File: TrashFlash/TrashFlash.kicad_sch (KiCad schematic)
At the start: 1 part, among them IC4 MCP4151-103E_MF

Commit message: Bevor new Shematic
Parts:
- removed IC4: MCP4151-103E_MF, SON65P300X300X100-9N-D, symbol TrashFlash:MCP4151-103E_MF
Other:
- added sheet MCU (MCU.kicad_sch)
- added sheet Supply (Supply.kicad_sch)
- sheet LED_Supply ports: added V_VOLTAGE_SET; removed POTY_CS, POTY_SCK, POTY_SDI/SDO

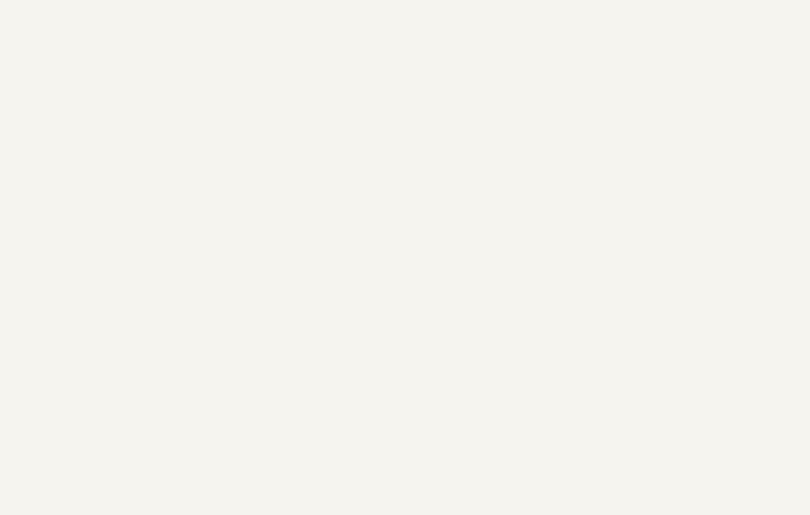
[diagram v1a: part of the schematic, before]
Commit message: Added RGB leds/driver for user interface
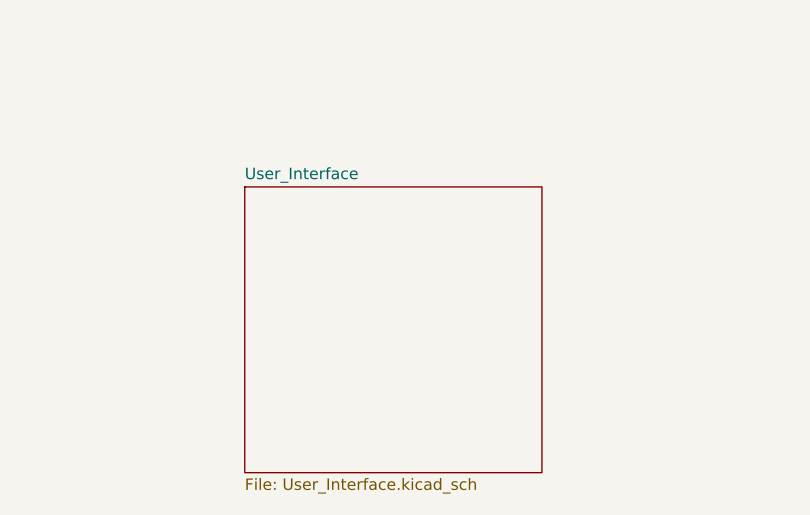
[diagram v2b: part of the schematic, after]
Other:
- added sheet User_Interface (User_Interface.kicad_sch)
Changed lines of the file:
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@@
+		)
+	)
+	(sheet
+		(at 121.92 124.46)
+		(size 33.02 31.75)
+		(exclude_from_sim no)
+		(in_bom yes)
+		(on_board yes)
+		(dnp no)
+		(fields_autoplaced yes)
+		(stroke
+			(width 0.1524)
+			(type solid)
+		)
+		(fill
+			(color 0 0 0 0.0000)
+		)
+		(property "Sheetname" "User_Interface"
+			(at 121.92 123.7484 0)
+			(effects
+				(font
+					(size 1.27 1.27)
+				)
+				(justify left bottom)
+			)
+		)
+		(property "Sheetfile" "User_Interface.kicad_sch"
+			(at 121.92 156.7946 0)
+			(effects
+				(font
+					(size 1.27 1.27)
+				)
+				(justify left top)
+			)
+		)
+		(instances
+			(project "TrashFlash"
+				(path "/256082dc-9c82-41ae-bfb7-0b4bd4121c78"
+					(page "6")
+				)
+			)
 		)
 	)

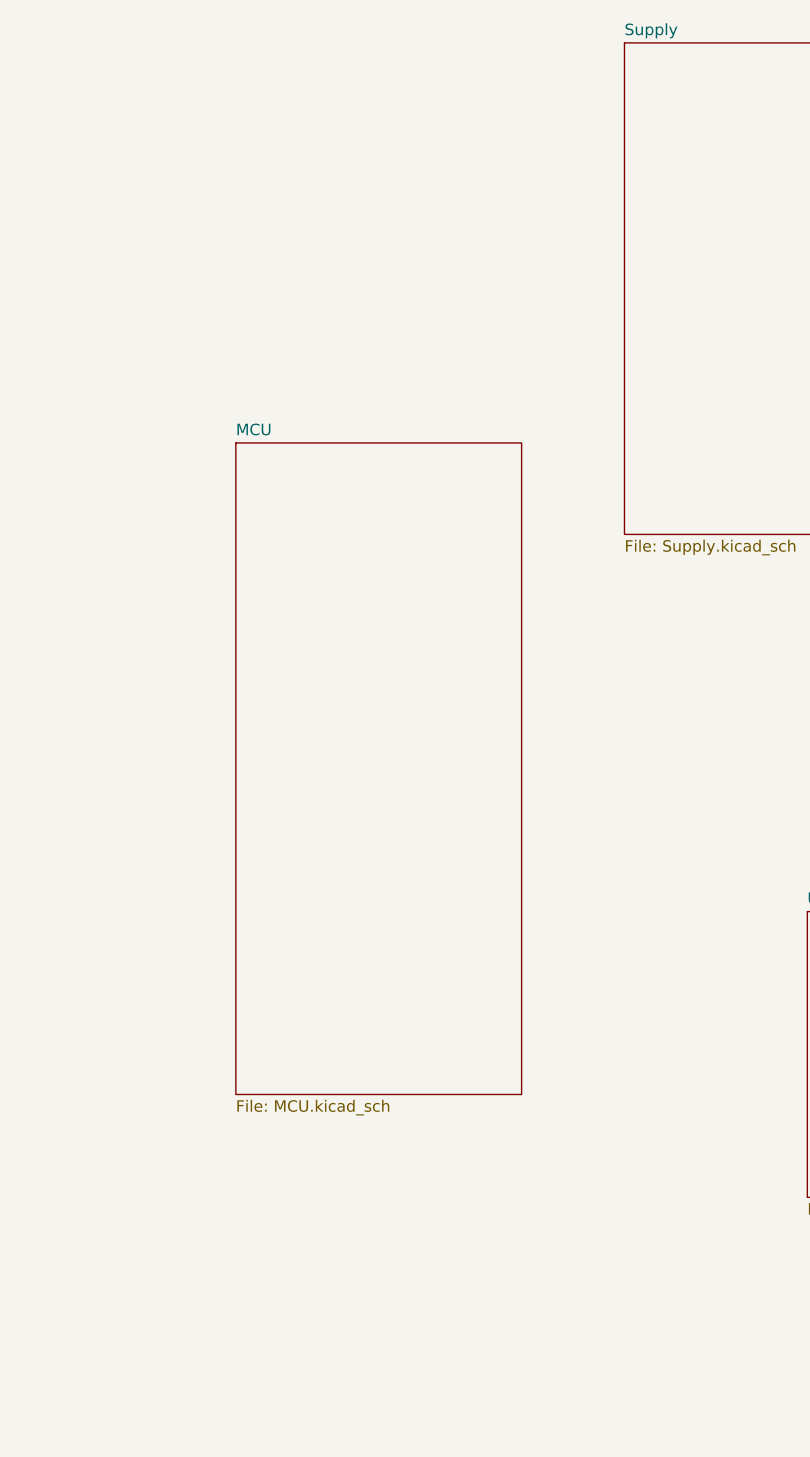
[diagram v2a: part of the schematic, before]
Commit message: Added Battery Management
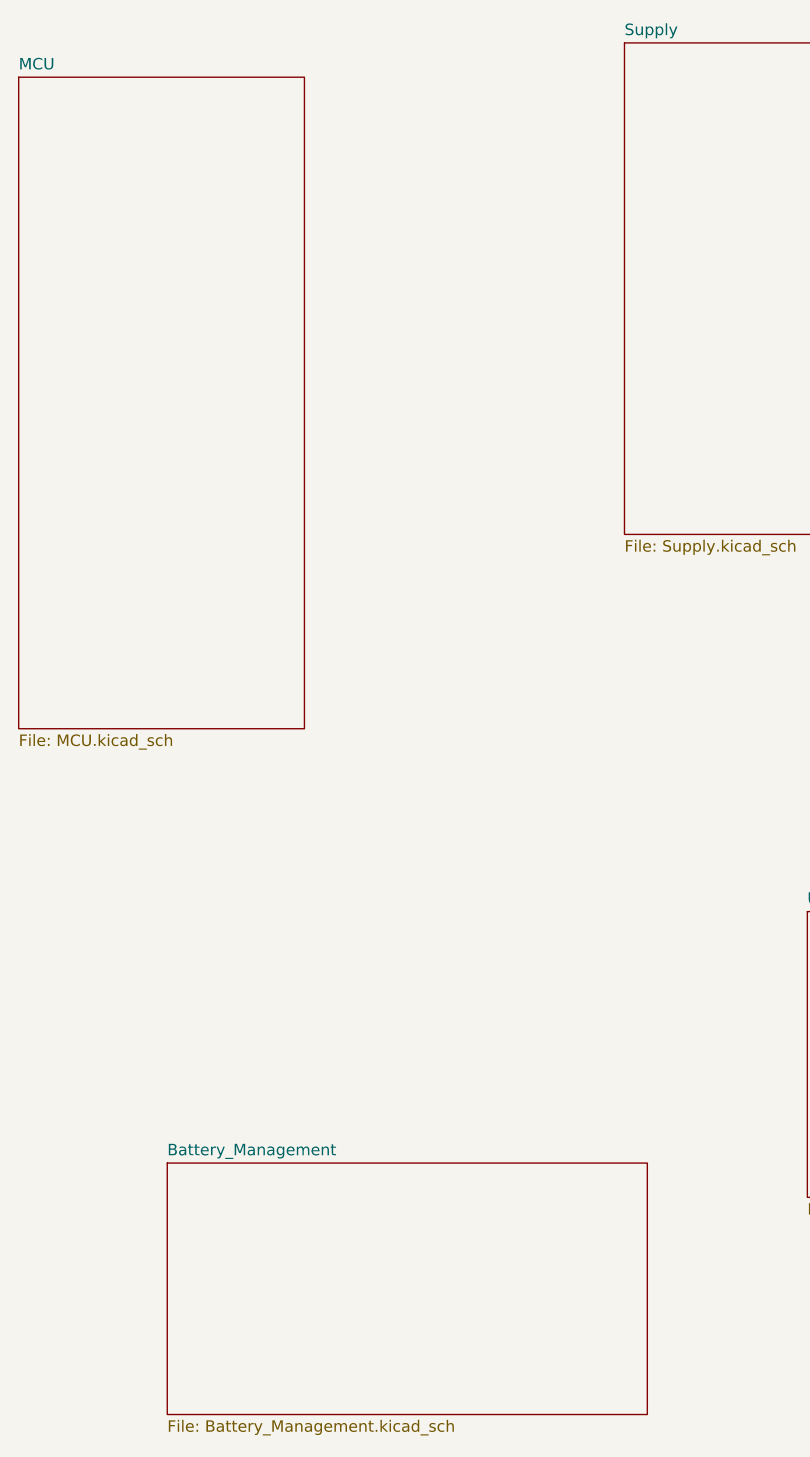
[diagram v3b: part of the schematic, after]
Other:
- added sheet Battery_Management (Battery_Management.kicad_sch)
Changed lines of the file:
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@@
 	)
 	(sheet
-		(at 58.42 72.39)
+		(at 50.8 152.4)
+		(size 53.34 27.94)
+		(exclude_from_sim no)
+		(in_bom yes)
+		(on_board yes)
+		(dnp no)
+		(fields_autoplaced yes)
+		(stroke
+			(width 0.1524)
+			(type solid)
+		)
+		(fill
+			(color 0 0 0 0.0000)
+		)
+		(property "Sheetname" "Battery_Management"
+			(at 50.8 151.6884 0)
+			(effects
+				(font
+					(size 1.27 1.27)
+				)
+				(justify left bottom)
+			)
+		)
+		(property "Sheetfile" "Battery_Management.kicad_sch"
+			(at 50.8 180.9246 0)
+			(effects
+				(font
+					(size 1.27 1.27)
+				)
+				(justify left top)
+			)
+		)
+		(instances
+			(project "TrashFlash"
+				(path "/256082dc-9c82-41ae-bfb7-0b4bd4121c78"
+					(page "7")
+				)
+			)
+		)
+	)
+	(sheet
+		(at 34.29 31.75)
 		(size 31.75 72.39)
 		(exclude_from_sim no)
@@
 		)
 		(property "Sheetname" "MCU"
-			(at 58.42 71.6784 0)
+			(at 34.29 31.0384 0)
 			(effects
 				(font
@@
 		)
 		(property "Sheetfile" "MCU.kicad_sch"
-			(at 58.42 145.3646 0)
+			(at 34.29 104.7246 0)
 			(effects
 				(font

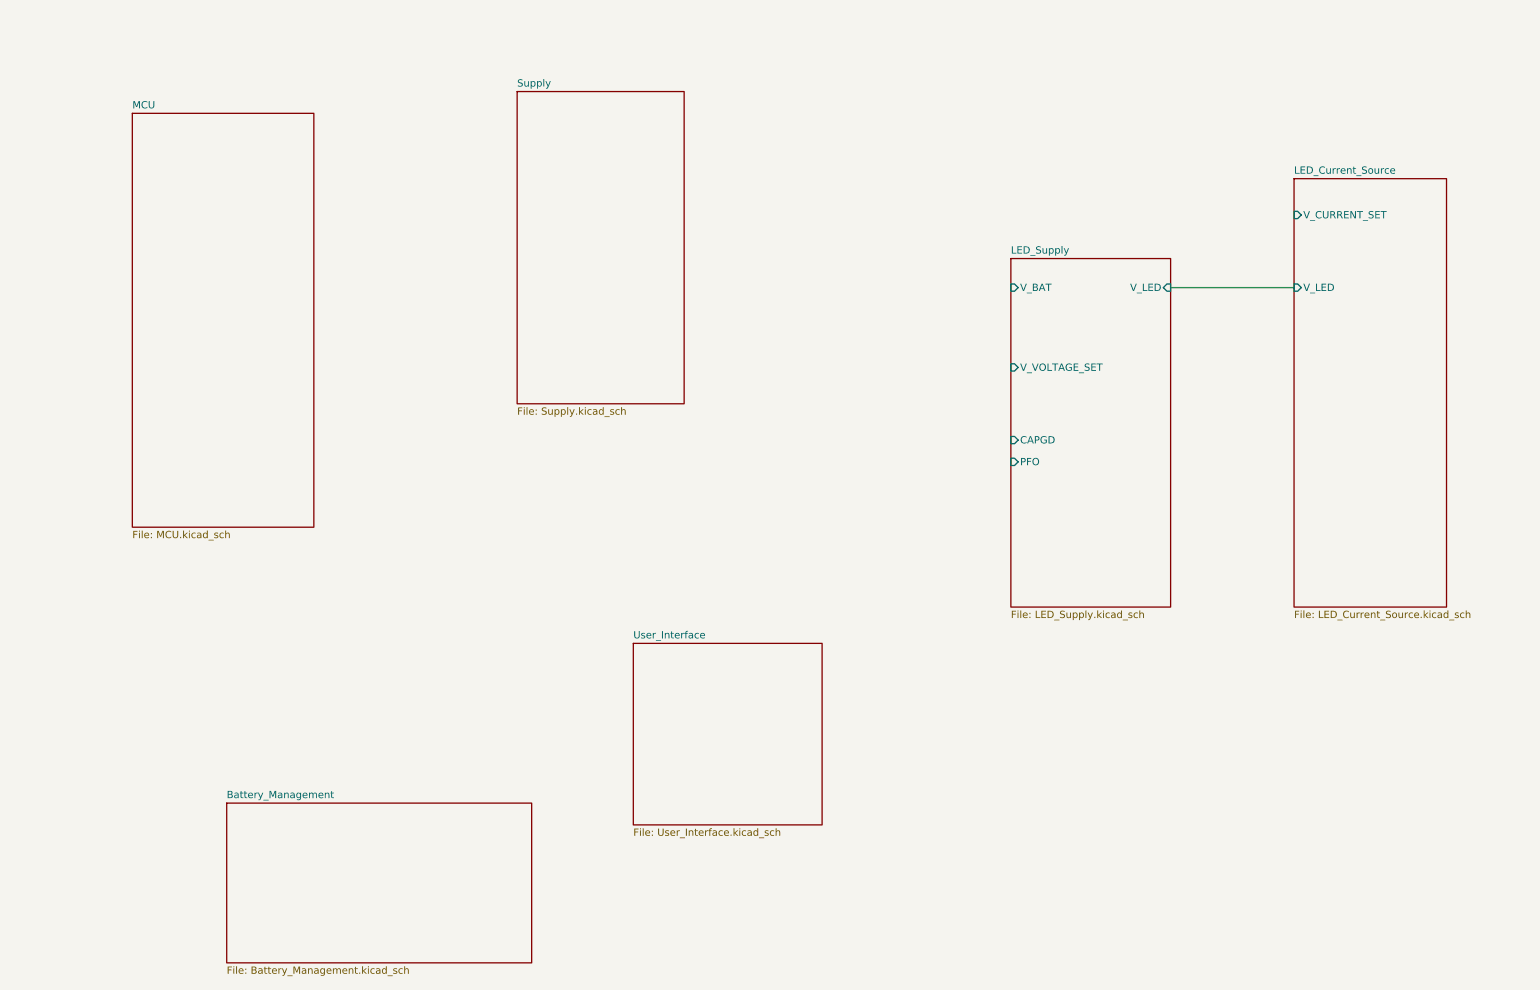
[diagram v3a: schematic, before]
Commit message: Added USB and powernets
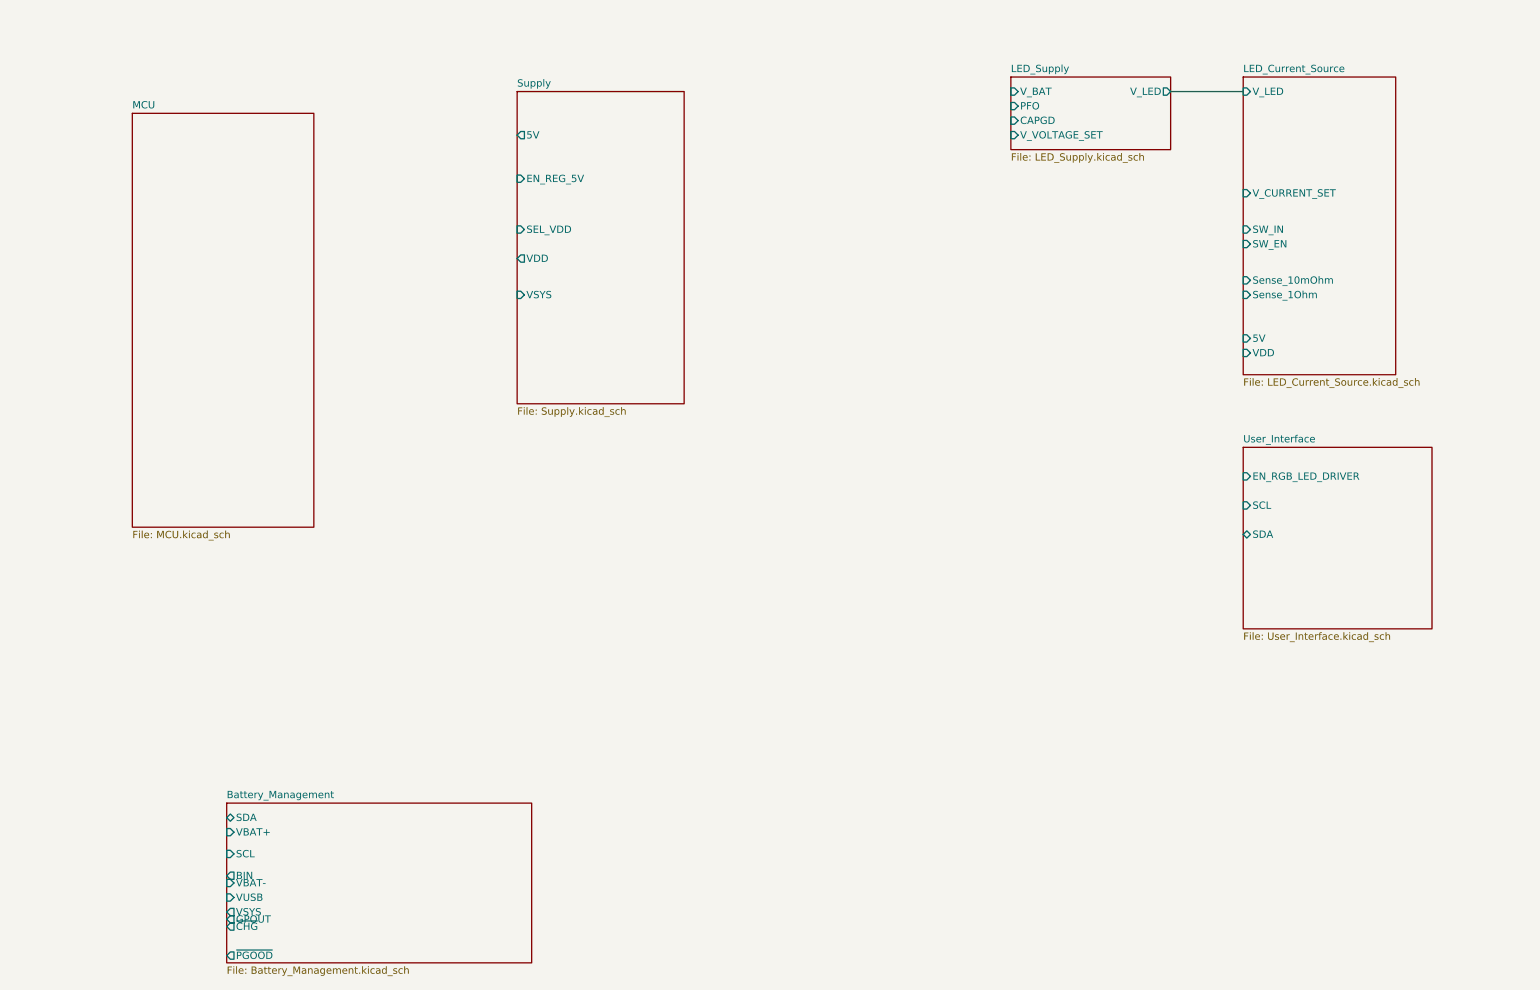
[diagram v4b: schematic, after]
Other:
- sheet Battery_Management ports: added BIN, GPOUT, SCL, SDA, VBAT+, VBAT-, VSYS, VUSB, ~{CHG}, ~{PGOOD}; removed none
- sheet LED_Current_Source ports: added 5V, SW_EN, SW_IN, Sense_10mOhm, Sense_1Ohm, VDD; removed none
- sheet Supply ports: added 5V, EN_REG_5V, SEL_VDD, VDD, VSYS; removed none
- sheet User_Interface ports: added EN_RGB_LED_DRIVER, SCL, SDA; removed none

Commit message: Added Wireless and inter PCB connector
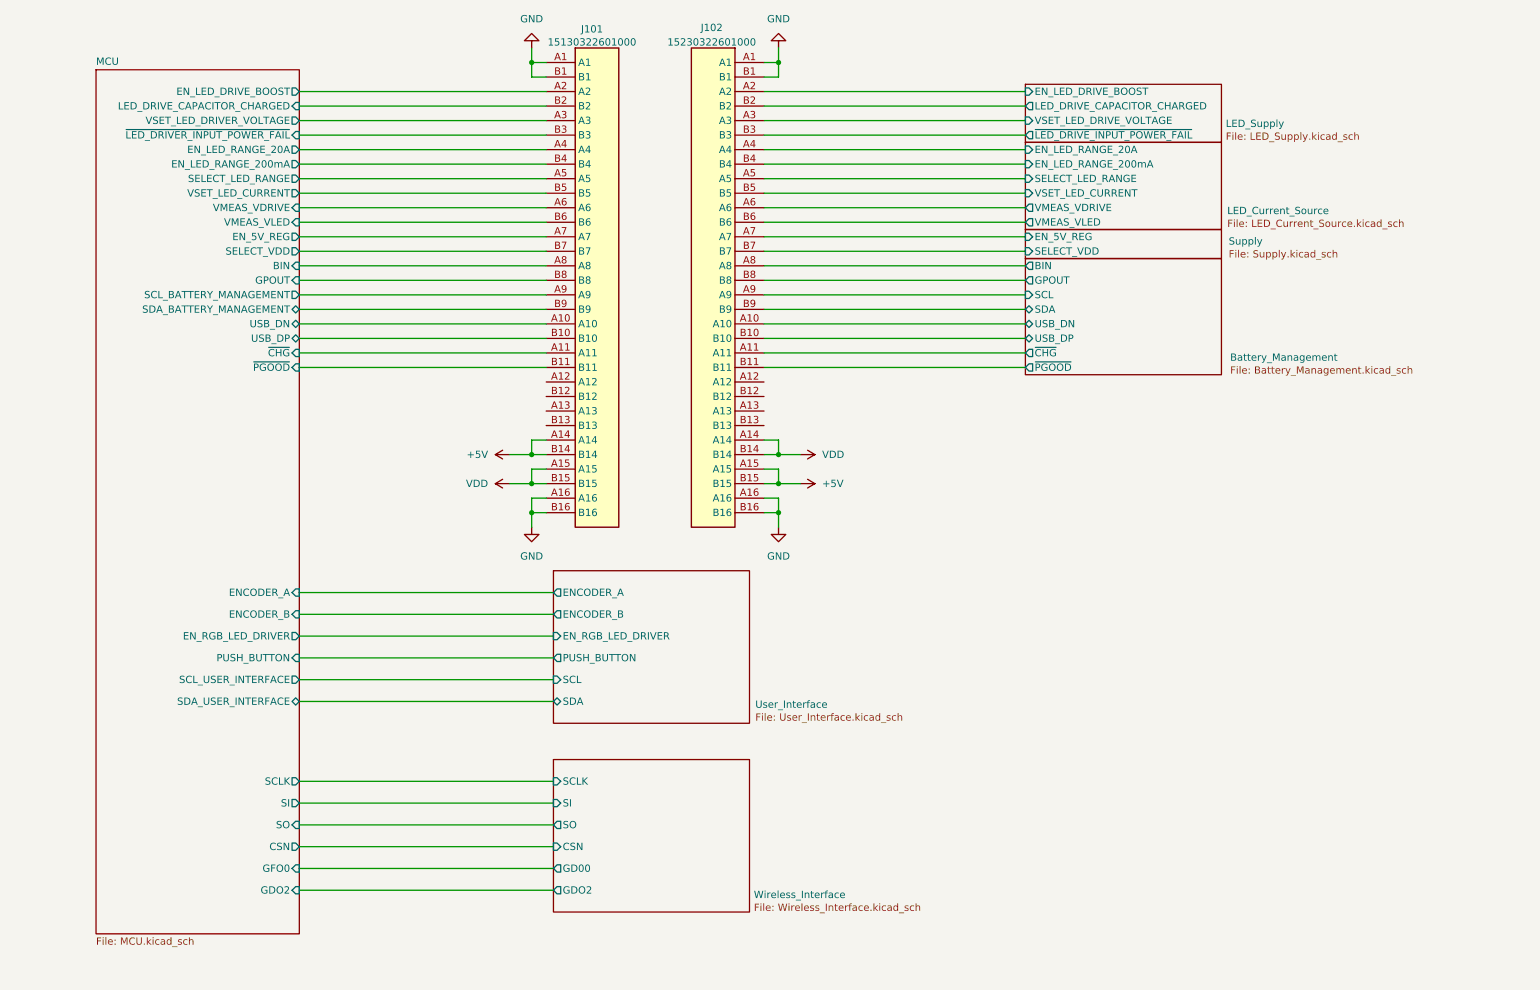
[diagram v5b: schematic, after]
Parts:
- added J101: 15130322601000, 15130322601000, symbol TrashFlash:15130322601000
- added J102: 15230322601000, 15230322601000, symbol TrashFlash:15230322601000
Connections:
- net Battery_Management/BIN: now also J102.A8
- net Battery_Management/GPOUT: now also J102.B8
- net Battery_Management/SCL: now also J102.A9
- net Battery_Management/SDA: now also J102.B9
- net Battery_Management/~{CHG}: now also J102.A11
- net Battery_Management/~{PGOOD}: now also J102.B11
- new net +5V: J101.A14, J101.B14, J102.A15, J102.B15
- new net Battery_Management/USB_DN: J102.A10
- new net Battery_Management/USB_DP: J102.B10
- new net GND: J101.A1, J101.A16, J101.B1, J101.B16, J102.A1, J102.A16, J102.B1, J102.B16
- new net LED_Current_Source/EN_LED_RANGE_200mA: J102.B4
- new net LED_Current_Source/EN_LED_RANGE_20A: J102.A4
- new net LED_Current_Source/SELECT_LED_RANGE: J102.A5
- new net LED_Current_Source/VMEAS_VDRIVE: J102.A6
- new net LED_Current_Source/VMEAS_VLED: J102.B6
- new net LED_Current_Source/VSET_LED_CURRENT: J102.B5
- new net LED_Supply/EN_LED_DRIVE_BOOST: J102.A2
- new net LED_Supply/LED_DRIVE_CAPACITOR_CHARGED: J102.B2
- new net LED_Supply/VSET_LED_DRIVE_VOLTAGE: J102.A3
- new net LED_Supply/~{LED_DRIVE_INPUT_POWER_FAIL}: J102.B3
- new net MCU/BIN: J101.A8
- new net MCU/EN_5V_REG: J101.A7
- new net MCU/EN_LED_DRIVE_BOOST: J101.A2
- new net MCU/EN_LED_RANGE_200mA: J101.B4
- new net MCU/EN_LED_RANGE_20A: J101.A4
- new net MCU/GPOUT: J101.B8
- new net MCU/LED_DRIVE_CAPACITOR_CHARGED: J101.B2
- new net MCU/SCL_BATTERY_MANAGEMENT: J101.A9
- new net MCU/SDA_BATTERY_MANAGEMENT: J101.B9
- new net MCU/SELECT_LED_RANGE: J101.A5
- new net MCU/SELECT_VDD: J101.B7
- new net MCU/USB_DN: J101.A10
- new net MCU/USB_DP: J101.B10
- new net MCU/VMEAS_VDRIVE: J101.A6
- new net MCU/VMEAS_VLED: J101.B6
- new net MCU/VSET_LED_CURRENT: J101.B5
- new net MCU/VSET_LED_DRIVER_VOLTAGE: J101.A3
- new net MCU/~{CHG}: J101.A11
- new net MCU/~{LED_DRIVER_INPUT_POWER_FAIL}: J101.B3
- new net MCU/~{PGOOD}: J101.B11
- new net Supply/EN_5V_REG: J102.A7
- new net Supply/SELECT_VDD: J102.B7
- new net VDD: J101.A15, J101.B15, J102.A14, J102.B14
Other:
- added sheet Wireless_Interface (Wireless_Interface.kicad_sch)
- sheet Battery_Management ports: added USB_DN, USB_DP; removed VBAT+, VBAT-, VSYS, VUSB
- sheet LED_Current_Source ports: added EN_LED_RANGE_200mA, EN_LED_RANGE_20A, SELECT_LED_RANGE, VMEAS_VDRIVE, VMEAS_VLED, VSET_LED_CURRENT; removed 5V, SW_EN, SW_IN, Sense_10mOhm, Sense_1Ohm, VDD, V_CURRENT_SET, V_LED
- sheet LED_Supply ports: added EN_LED_DRIVE_BOOST, LED_DRIVE_CAPACITOR_CHARGED, VSET_LED_DRIVE_VOLTAGE, ~{LED_DRIVE_INPUT_POWER_FAIL}; removed CAPGD, PFO, V_BAT, V_LED, V_VOLTAGE_SET
- sheet MCU ports: added BIN, CSN, ENCODER_A, ENCODER_B, EN_5V_REG, EN_LED_DRIVE_BOOST, EN_LED_RANGE_200mA, EN_LED_RANGE_20A, EN_RGB_LED_DRIVER, GDO2, GFO0, GPOUT, LED_DRIVE_CAPACITOR_CHARGED, PUSH_BUTTON, SCLK, SCL_BATTERY_MANAGEMENT, SCL_USER_INTERFACE, SDA_BATTERY_MANAGEMENT, SDA_USER_INTERFACE, SELECT_LED_RANGE, SELECT_VDD, SI, SO, USB_DN, USB_DP, VMEAS_VDRIVE, VMEAS_VLED, VSET_LED_CURRENT, VSET_LED_DRIVER_VOLTAGE, ~{CHG}, ~{LED_DRIVER_INPUT_POWER_FAIL}, ~{PGOOD}; removed none
- sheet Supply ports: added EN_5V_REG, SELECT_VDD; removed 5V, EN_REG_5V, SEL_VDD, VDD, VSYS
- sheet User_Interface ports: added ENCODER_A, ENCODER_B, PUSH_BUTTON; removed none

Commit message: Stackup changed, Led placement adjusted
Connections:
- no-connect marks 0 -> 8
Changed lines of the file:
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@@
 		(color 0 0 0 0)
+	)
+	(no_connect
+		(at 144.78 81.28)
+	)
+	(no_connect
+		(at 144.78 78.74)
+	)
+	(no_connect
+		(at 144.78 86.36)
+	)
+	(no_connect
+		(at 106.68 81.28)
+	)
+	(no_connect
+		(at 106.68 83.82)
+	)
+	(no_connect
+		(at 106.68 78.74)
+	)
+	(no_connect
+		(at 106.68 86.36)
+	)
+	(no_connect
+		(at 144.78 83.82)
 	)
 	(wire
